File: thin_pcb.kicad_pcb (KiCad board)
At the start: 2 copper layers, 95.2 x 95.2 mm, 127 parts, among them J01 Conn_01x02, J02 Conn_01x02, J04 Conn_01x02, J06 Conn_01x02, J07 Conn_01x02, J08 Conn_01x02, J1 USB_B_Micro, J11 Conn_01x03, J12 Conn_01x03, J13 Conn_01x03, J14 Conn_01x03, J15 Conn_01x03, J16 Conn_01x03, J17 Conn_01x03, J18 Conn_01x03, J2 AudioJack4_Ground, J21 Conn_01x07, J22 Conn_01x07, J23 Conn_01x07, J24 Conn_01x07, J25 Conn_01x07, J26 Conn_01x07, J27 Conn_01x07, J28 Conn_01x07, J3 AudioJack4_Ground, J31 Conn_01x07, J32 Conn_01x07, J33 Conn_01x07, J34 Conn_01x07, J35 Conn_01x07, J36 Conn_01x07, J37 Conn_01x07, J38 Conn_01x07, J4 Conn_01x06, J41 Conn_01x04, J42 Conn_01x04, J43 Conn_01x04, J44 Conn_01x04, J45 Conn_01x04, J46 Conn_01x04, J47 Conn_01x04, J48 Conn_01x04, J5 Conn_01x06, J51 Conn_01x01, J52 Conn_01x01, J53 Conn_01x01, J54 Conn_01x01, J55 Conn_01x01, J56 Conn_01x01, J57 Conn_01x01, J58 Conn_01x01, J6 Conn_02x02, J7 Conn_01x02, SW11 SW_Push, SW12 SW_Push, SW13 SW_Push, SW14 SW_Push, SW15 SW_Push, SW21 SW_Push, SW22 SW_Push, SW23 SW_Push, SW24 SW_Push, SW25 SW_Push, SW252 SW_Push, SW31 SW_Push, SW32 SW_Push, SW33 SW_Push, SW34 SW_Push, SW35 SW_Push, SW41 SW_Push, SW42 SW_Push, SW422 SW_Push, SW43 SW_Push, SW44 SW_Push, SW45 SW_Push, SW452 SW_Push, SW51 SW_Push, SW52 SW_Push, SW522 SW_Push, SW53 SW_Push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

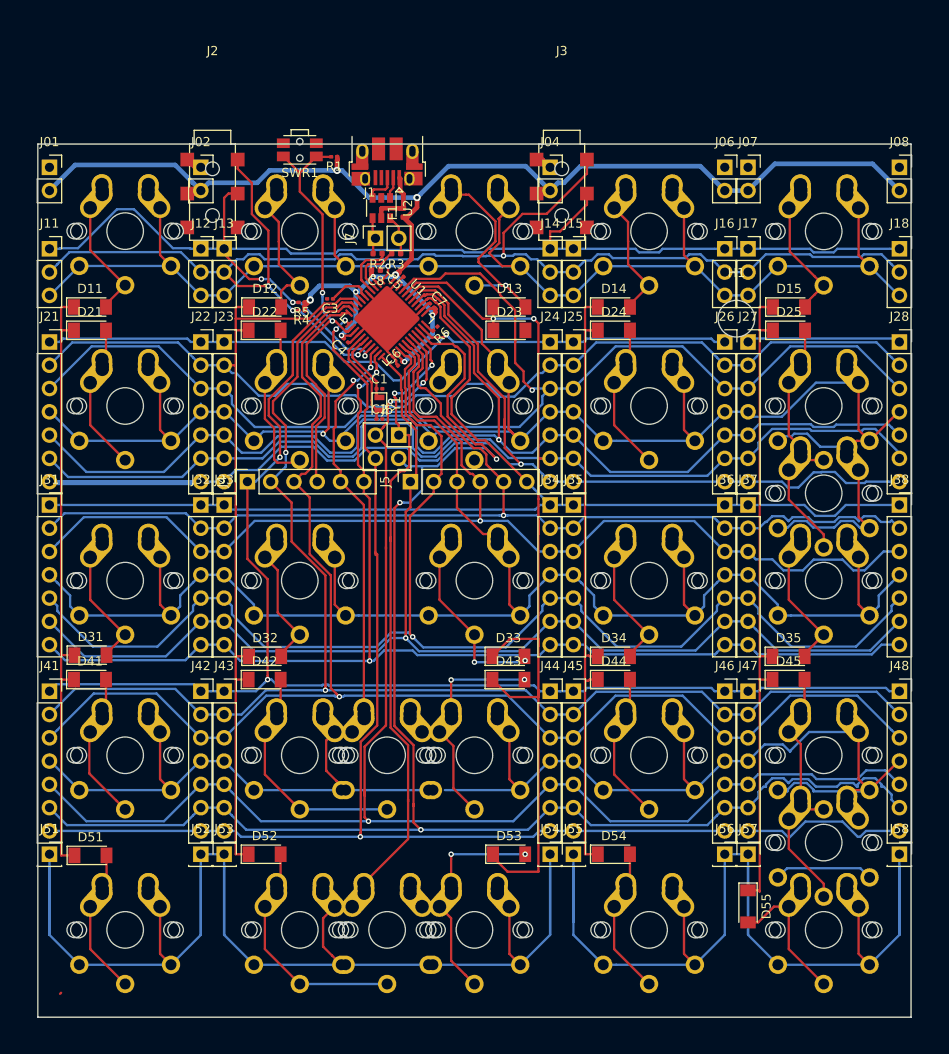
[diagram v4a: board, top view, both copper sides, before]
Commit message: fix circuits labels
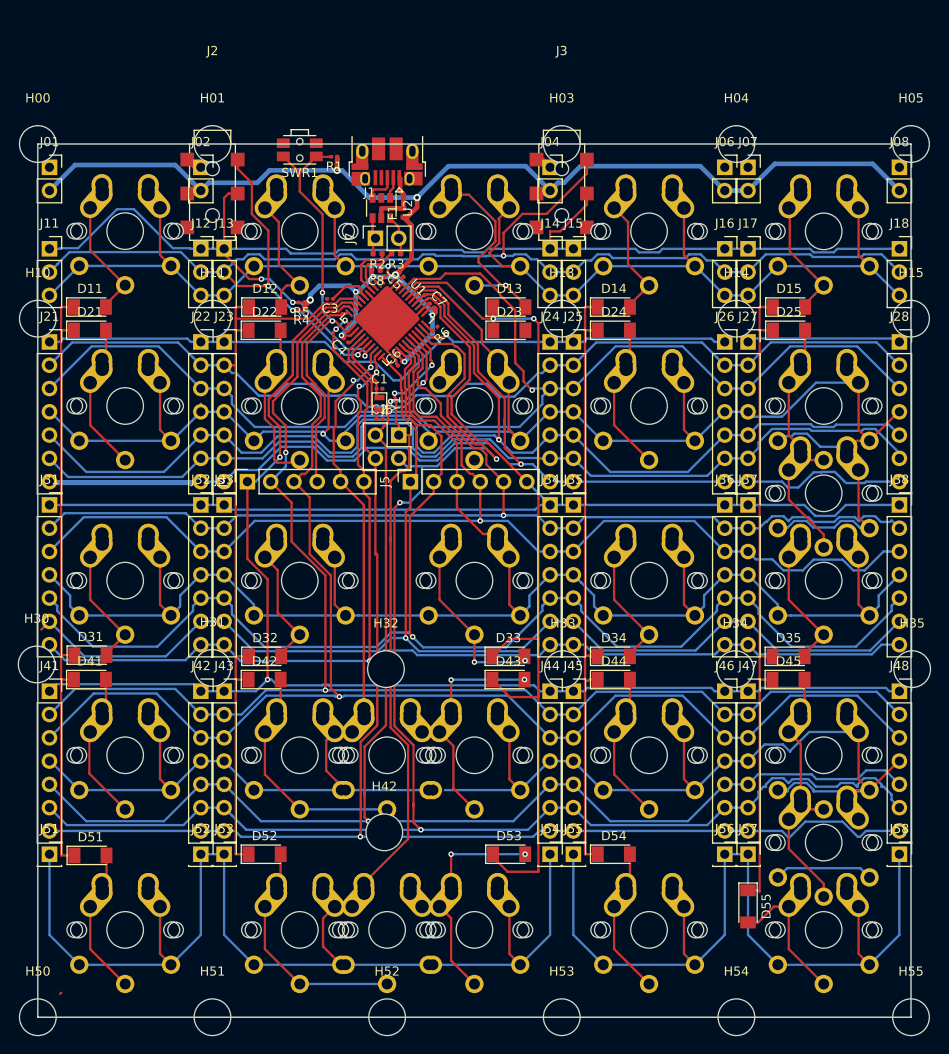
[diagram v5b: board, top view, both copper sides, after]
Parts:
- removed H1: MountingHole, MountingHole:MountingHole_4mm
- added H00: MountingHole, MountingHole:MountingHole_4mm, F.Cu at (51.4, 59.1)
- added H01: MountingHole, MountingHole:MountingHole_4mm, F.Cu at (70.5, 59.1)
- added H03: MountingHole, MountingHole:MountingHole_4mm, F.Cu at (108.6, 59.1)
- added H04: MountingHole, MountingHole:MountingHole_4mm, F.Cu at (127.6, 59.1)
- added H05: MountingHole, MountingHole:MountingHole_4mm, F.Cu at (146.7, 59.1)
- added H10: MountingHole, MountingHole:MountingHole_4mm, F.Cu at (51.4, 78.1)
- added H11: MountingHole, MountingHole:MountingHole_4mm, F.Cu at (70.5, 78.1)
- added H13: MountingHole, MountingHole:MountingHole_4mm, F.Cu at (108.6, 78.1)
- added H14: MountingHole, MountingHole:MountingHole_4mm, F.Cu at (127.6, 78.1)
- added H15: MountingHole, MountingHole:MountingHole_4mm, F.Cu at (146.7, 78.1)
- added H30: MountingHole, MountingHole:MountingHole_4mm, F.Cu at (51.3, 115.8)
- added H31: MountingHole, MountingHole:MountingHole_4mm, F.Cu at (70.5, 116.2)
- added H32: MountingHole, MountingHole:MountingHole_4mm, F.Cu at (89.4, 116.3)
- added H33: MountingHole, MountingHole:MountingHole_4mm, F.Cu at (108.7, 116.3)
- added H34: MountingHole, MountingHole:MountingHole_4mm, F.Cu at (127.5, 116.3)
- added H35: MountingHole, MountingHole:MountingHole_4mm, F.Cu at (146.8, 116.3)
- added H42: MountingHole, MountingHole:MountingHole_4mm, F.Cu at (89.2, 134.1)
- added H50: MountingHole, MountingHole:MountingHole_4mm, F.Cu at (51.4, 154.3)
- added H51: MountingHole, MountingHole:MountingHole_4mm, F.Cu at (70.5, 154.3)
- added H52: MountingHole, MountingHole:MountingHole_4mm, F.Cu at (89.5, 154.3)
- added H53: MountingHole, MountingHole:MountingHole_4mm, F.Cu at (108.6, 154.3)
- added H54: MountingHole, MountingHole:MountingHole_4mm, F.Cu at (127.6, 154.3)
- added H55: MountingHole, MountingHole:MountingHole_4mm, F.Cu at (146.7, 154.3)
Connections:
- net COL3 renamed F1
- net COL4 renamed D5
- net COL5 renamed B2
- net MISO renamed B3
- net SCL renamed D0
- net SCLK renamed B1
- net SDA renamed D1
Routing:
- net COL4: track 0.00 -> 139.0 mm, vias 0 -> 1
- net D5: track 204.5 -> 66.8 mm, vias 1 -> 0
- net B6: track 326.5 -> 275.2 mm

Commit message: reset pinhole
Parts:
- moved H42 1.16 mm to (89.5, 135.3)
- moved H33 0.18 mm to (108.6, 116.2)
- moved H34 0.16 mm to (127.6, 116.2)
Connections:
- J4 pad 1: B1 -> RESET
- J4 pad 2: B2 -> B1
- J4 pad 3: B3 -> B2
- J4 pad 4: RESET -> B3
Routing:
- net COL4: track 139.0 -> 0.00 mm, vias 1 -> 0
- net D5: track 66.8 -> 202.1 mm, vias 0 -> 1
- net F5: track 158.5 -> 127.7 mm
- net D2: track 203.2 -> 219.4 mm
- net D4: track 150.8 -> 140.9 mm
- net D6: track 174.5 -> 181.7 mm
- net B6: track 275.2 -> 280.2 mm
- net RESET: track 47.7 -> 51.5 mm, vias 2 -> 4
- net C7: track 98.5 -> 101.0 mm
- net B7: track 155.9 -> 158.0 mm
- net B5: track 163.5 -> 161.7 mm
- net B2: track 222.7 -> 224.1 mm, vias 2 -> 1
- net B3: track 157.6 -> 156.3 mm
- net D3: track 133.4 -> 132.4 mm
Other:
- rule trace_min: 0.2 -> 0.127
- rule via_min_size: 0.45 -> 0.3

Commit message: breakline
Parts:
- added REF**: BreakLine_2x7, lib:BreakLine_2x7, F.Cu at (108.6, 80.6)
- added REF**: BreakLine_2, lib:BreakLine_2, F.Cu at (70.5, 64.8)
- added REF**: BreakLine_2, lib:BreakLine_2, F.Cu at (108.6, 64.1)
- added REF**: BreakLine_2x4, lib:BreakLine_2x4, F.Cu at (108.6, 67.9)
- added REF**: BreakLine_2x7, lib:BreakLine_2x7, F.Cu at (71.8, 97.2)
- added REF**: BreakLine_2x7, lib:BreakLine_2x7, F.Cu at (92.1, 97.2)
- added REF**: BreakLine_2, lib:BreakLine_2, F.Cu at (89.5, 97.2)
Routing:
- net B2: track 224.1 -> 233.5 mm
- net D2: track 219.4 -> 228.7 mm
- net D0: track 152.9 -> 161.7 mm
- net B3: track 156.3 -> 165.0 mm
- net B1: track 145.1 -> 153.5 mm
- net F6: track 132.4 -> 140.0 mm
- net C7: track 101.0 -> 108.6 mm
- net F5: track 127.7 -> 135.3 mm
- net E6: track 142.3 -> 150.0 mm
- net F0: track 136.5 -> 144.1 mm
- net B0: track 187.9 -> 195.6 mm
- net F1: track 208.9 -> 216.4 mm
- net B7: track 158.0 -> 165.2 mm
- net C6: track 178.9 -> 185.9 mm
- net F4: track 188.9 -> 195.6 mm
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
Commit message: breaklines
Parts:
- removed the REF** at (70.5, 64.8)
- added REF**: BreakLine_2, lib:BreakLine_2, F.Cu at (127.6, 64.1)
- added REF**: BreakLine_2x7, lib:BreakLine_2x7, F.Cu at (108.6, 98.4)
- added REF**: BreakLine_2x7, lib:BreakLine_2x7, F.Cu at (127.6, 98.4)
- added REF**: BreakLine_2x7, lib:BreakLine_2x7, F.Cu at (127.6, 80.6)
- added REF**: BreakLine_2_13.43_2, lib:BreakLine_2_13.43_2, F.Cu at (127.6, 153.0)
- added REF**: BreakLine_2_13.43_2, lib:BreakLine_2_13.43_2, F.Cu at (108.6, 153.0)
- added REF**: BreakLine_2_13.43_2, lib:BreakLine_2_13.43_2, F.Cu at (70.5, 153.0)
- added REF**: BreakLine_2_13.43_2, lib:BreakLine_2_13.43_2, F.Cu at (128.9, 78.1)
- added REF**: BreakLine_2_13.43_2, lib:BreakLine_2_13.43_2, F.Cu at (109.9, 78.1)
- added REF**: BreakLine_2_13.43_2, lib:BreakLine_2_13.43_2, F.Cu at (109.9, 97.2)
- added REF**: BreakLine_2_13.43_2, lib:BreakLine_2_13.43_2, F.Cu at (128.9, 116.2)
- added REF**: BreakLine_2, lib:BreakLine_2, F.Cu at (70.5, 64.1)
- added REF**: BreakLine_2_13.43_2, lib:BreakLine_2_13.43_2, F.Cu at (109.9, 116.2)
- added REF**: BreakLine_2_13.43_2, lib:BreakLine_2_13.43_2, F.Cu at (109.9, 135.3)
- added REF**: BreakLine_2_13.43_2, lib:BreakLine_2_13.43_2, F.Cu at (90.8, 135.3)
- added REF**: BreakLine_2_13.43_2, lib:BreakLine_2_13.43_2, F.Cu at (71.8, 135.3)
- added REF**: BreakLine_2_13.43_2, lib:BreakLine_2_13.43_2, F.Cu at (52.7, 135.3)
- added REF**: BreakLine_2_13.43_2, lib:BreakLine_2_13.43_2, F.Cu at (52.7, 116.2)
- added REF**: BreakLine_2x7, lib:BreakLine_2x7, F.Cu at (92.1, 116.2)
- added REF**: BreakLine_2x4, lib:BreakLine_2x4, F.Cu at (70.5, 67.9)
- added REF**: BreakLine_2_13.43_2, lib:BreakLine_2_13.43_2, F.Cu at (52.7, 97.2)
- added REF**: BreakLine_2_13.43_2, lib:BreakLine_2_13.43_2, F.Cu at (52.7, 78.1)
- added REF**: BreakLine_2x7, lib:BreakLine_2x7, F.Cu at (71.8, 116.2)
- added REF**: BreakLine_2, lib:BreakLine_2, F.Cu at (127.6, 61.6)
- added REF**: BreakLine_2x4, lib:BreakLine_2x4, F.Cu at (127.6, 67.9)
- added REF**: BreakLine_2x7, lib:BreakLine_2x7, F.Cu at (70.5, 80.6)
- added REF**: BreakLine_2x7, lib:BreakLine_2x7, F.Cu at (70.5, 98.4)
- added REF**: BreakLine_2x7, lib:BreakLine_2x7, F.Cu at (70.5, 118.7)
- added REF**: BreakLine_2x7, lib:BreakLine_2x7, F.Cu at (127.6, 118.7)
- added REF**: BreakLine_2x7, lib:BreakLine_2x7, F.Cu at (108.6, 118.7)
- moved H30 0.40 mm to (51.4, 116.2)
- moved D12 0.26 mm to (76.2, 76.6)
- moved D21 0.26 mm to (57.1, 79.6)
- moved D11 0.26 mm to (57.1, 76.6)
- moved D43 0.15 mm to (102.8, 117.6)
- moved D55 0.15 mm to (129.0, 142.1)
- moved D33 0.15 mm to (102.8, 114.8)
- moved D41 0.14 mm to (57.2, 117.6)
- moved D44 0.14 mm to (114.3, 117.6)
- moved D45 0.14 mm to (133.4, 117.6)
- moved D24 0.14 mm to (114.3, 79.5)
- moved D34 0.14 mm to (114.3, 114.8)
- moved D35 0.14 mm to (133.4, 114.8)
- moved D52 0.14 mm to (76.2, 136.7)
- moved D54 0.14 mm to (114.3, 136.7)
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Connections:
- J41 pad 1: B1 -> B3
- J41 pad 3: B3 -> B1
- J42 pad 1: B1 -> B3
- J42 pad 3: B3 -> B1
- J43 pad 1: B1 -> B3
- J43 pad 3: B3 -> B1
- J44 pad 1: B1 -> B3
- J44 pad 3: B3 -> B1
- J45 pad 1: B1 -> B3
- J45 pad 3: B3 -> B1
- J46 pad 1: B1 -> B3
- J46 pad 3: B3 -> B1
- J47 pad 1: B1 -> B3
- J47 pad 3: B3 -> B1
- J48 pad 1: B1 -> B3
- J48 pad 3: B3 -> B1
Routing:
- net Net-(D23-Pad2): track 0.00 -> 25.0 mm, vias 0 -> 2
- net B1: track 153.5 -> 169.2 mm
- net B3: track 165.0 -> 149.7 mm
- net B6: track 280.1 -> 286.6 mm
- net C6: track 185.9 -> 192.4 mm
- net F7: track 131.0 -> 135.9 mm
- net D5: track 205.1 -> 210.0 mm
- net D7: track 133.0 -> 137.8 mm
- net D4: track 145.6 -> 150.3 mm
- net D6: track 185.0 -> 189.6 mm
- net VCC: track 163.5 -> 168.0 mm
- net D3: track 135.6 -> 139.9 mm
- net D2: track 228.7 -> 225.2 mm
- net B4: track 195.4 -> 198.0 mm
- net B5: track 168.1 -> 170.2 mm
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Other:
- net class Default: clearance 0.169333 -> 0.127
- rule trace_clearance: 0.169333 -> 0.127
